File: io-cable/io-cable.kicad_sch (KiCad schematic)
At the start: 6 parts, among them J101 0430251608, J2 0430251608

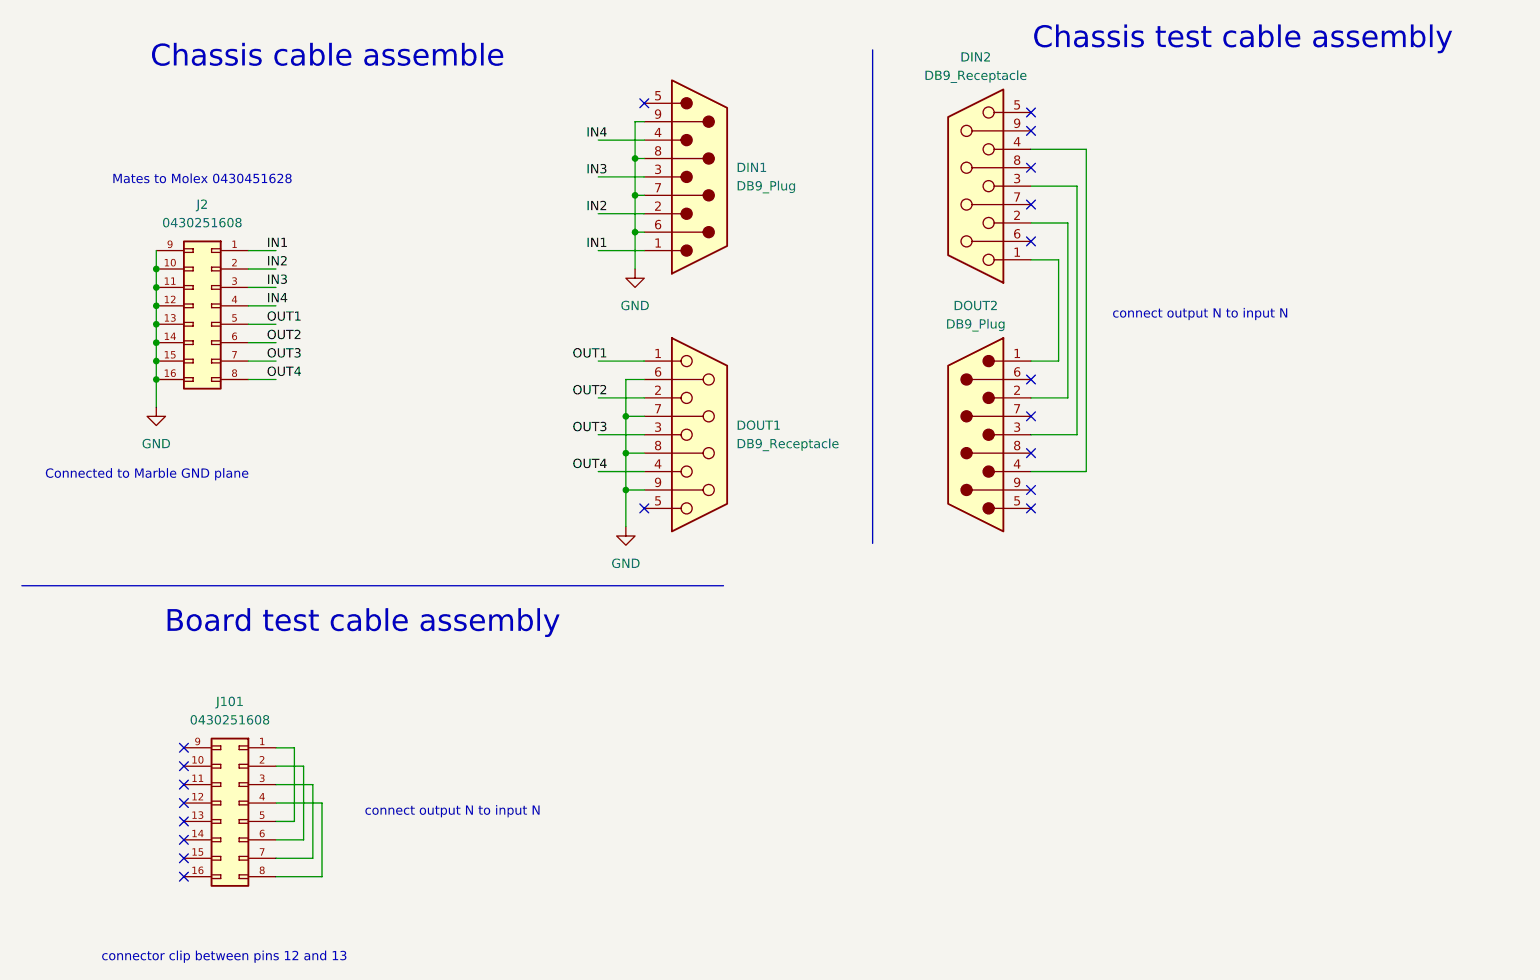
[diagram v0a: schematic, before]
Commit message: update io-cable
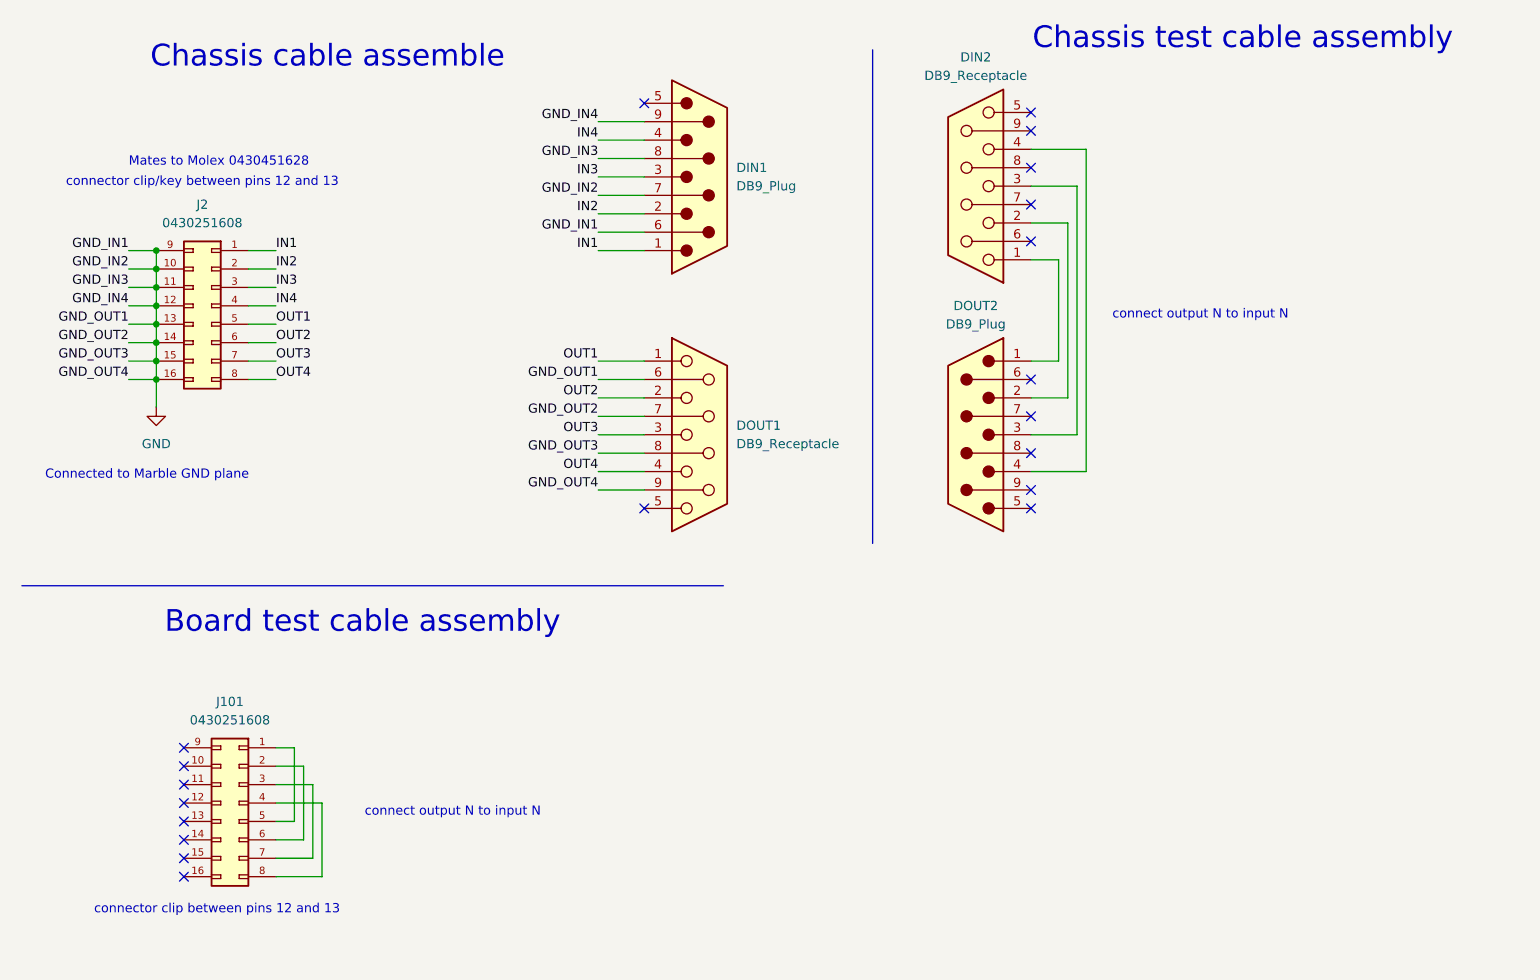
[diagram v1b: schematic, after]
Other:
- note added: "connector clip/key between pins 12 and 13"
